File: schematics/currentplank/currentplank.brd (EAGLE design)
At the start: 50 x 49 mm, 23 parts, among them IC1 74AHC1G86DBV, IC2 STCS2A, IC3 STCS2A, IC4 OPAMP-DUALU

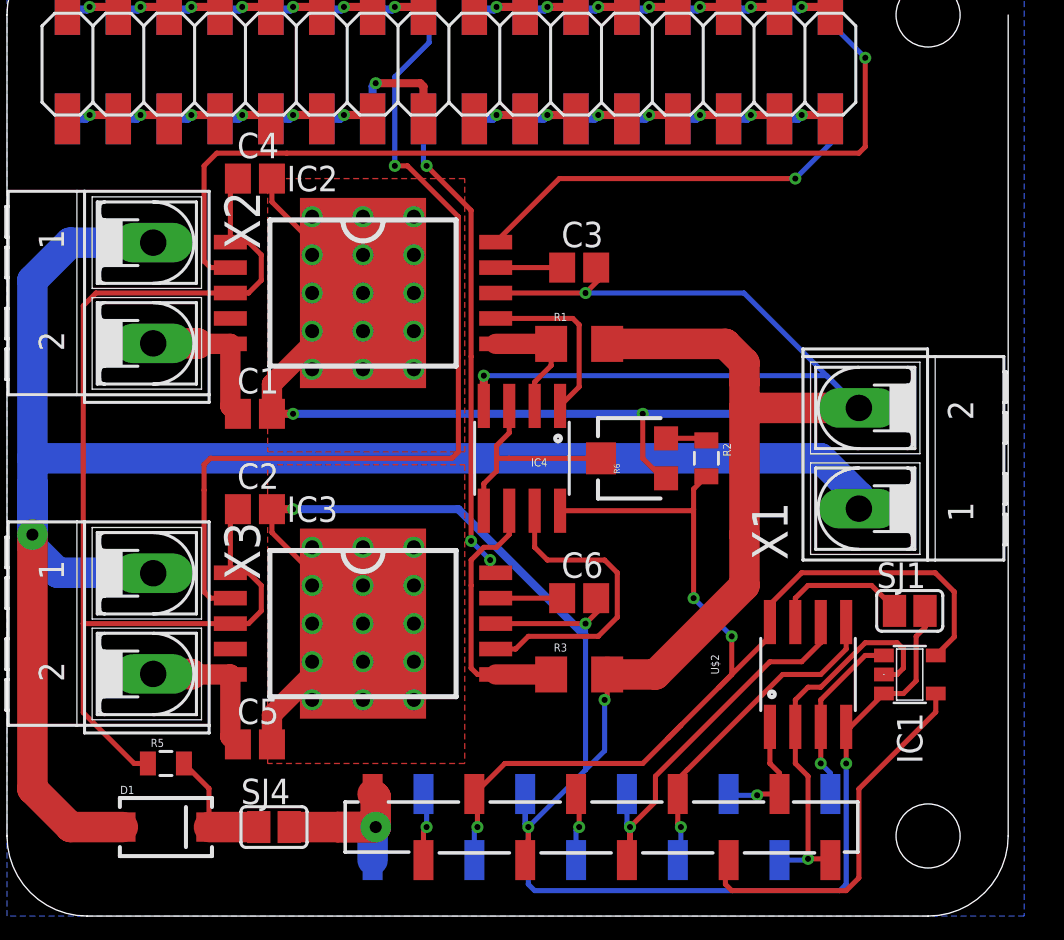
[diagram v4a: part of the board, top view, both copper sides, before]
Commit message: Updates to current plank silkscreen etc.
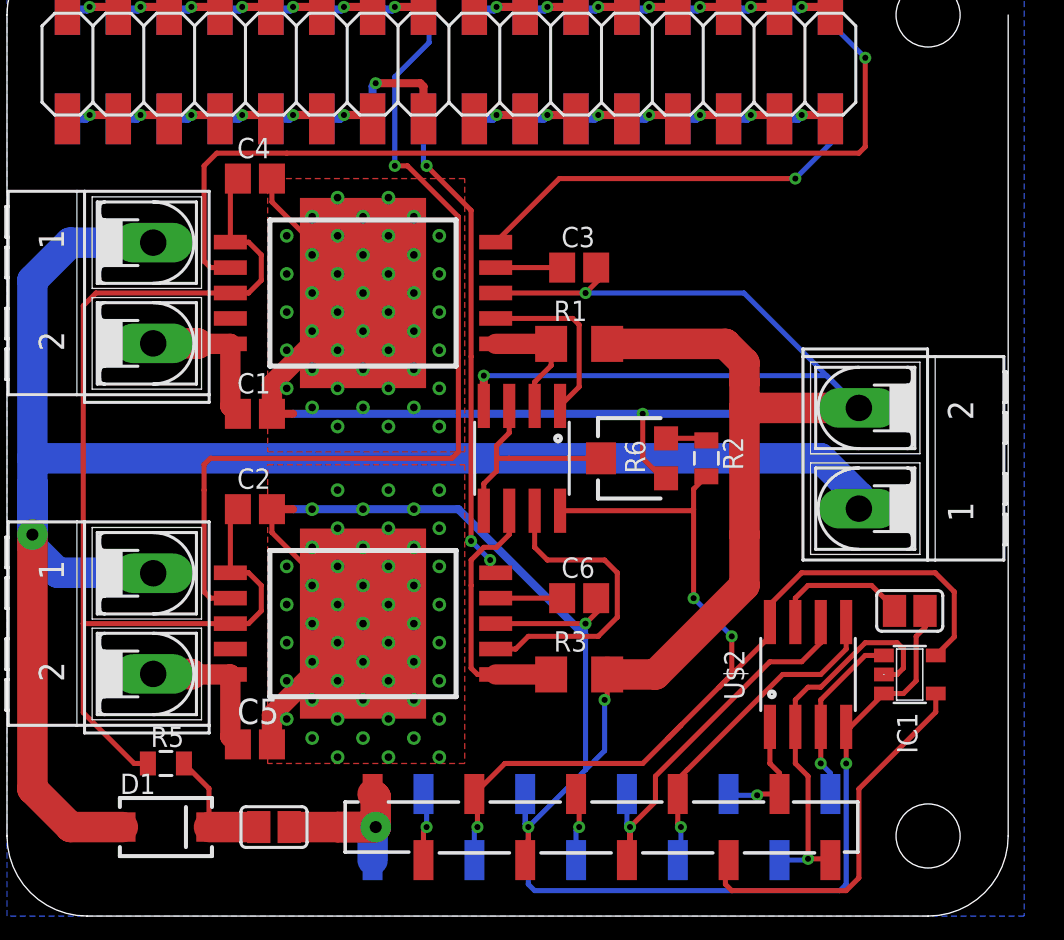
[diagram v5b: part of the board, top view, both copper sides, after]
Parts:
- IC4: value OPAMP-DUALU -> MCP6002
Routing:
- net GND: vias 39 -> 84

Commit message: Added logo to Current Plank, generated gerbers.
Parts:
- added U$3: (no value), SparkFun-Aesthetics:OSHW-LOGO-M
- added U$4: (no value), nickparts:ARACHNID_LABS_LOGO_SM
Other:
- board text added: "Loki LED Driver Plank v0.1"
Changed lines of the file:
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@@
 <board>
 <plain>
+<text x="25.0825" y="46.99" size="1.778" layer="25" align="bottom-center">Loki LED Driver Plank v0.1</text>
 </plain>
 <attributes>
@@
 <attribute name="NAME" x="35.7505" y="23.9395" size="1.016" layer="25" rot="R270"/>
 </element>
+<element name="U$3" library="SparkFun-Aesthetics" package="OSHW-LOGO-M" value="" x="34.29" y="33.655"/>
+<element name="U$4" library="nickparts" package="ARACHNID_LABS_LOGO_SM" value="" x="44.7675" y="33.655"/>
 </elements>
 <signals>
@@
 </signal>
 </signals>
+<errors>
+</errors>
 </board>
 </drawing>
